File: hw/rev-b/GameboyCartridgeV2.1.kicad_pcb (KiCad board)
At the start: 4 copper layers, 52.8 x 61.2 mm, 148 parts, among them J1 USB_C_Receptacle_USB2.0, J2 Micro_SD_Card_Det2, J4 Conn_01x06, J5 CartBus, Q1 CJ2302, Q101 SIA975DJ-T1-GE3, Q102 2N7002, SW1 SW_Push, SW2 SW_Push, U1 USBLC6-2P6, U101 TPS2116DRLR, U102 TPS2553DBVR, U103 TPS63802DLAR, U104 ESP32-C3-MINI-1U-N4, U105 SN74LVC1G125DBVR, U106 SN74LVC3G34DCTR, U107 CH334P, U108 TLV3012BIDBVR, U109 TLV431BIDBZR, U2 W25Q16JVSSIQ, U3 RP2350_80QFN, U4 W956A8MBYA5I, U5 MCP79510, U6 AP2112K-3.3, U7 TXB0108PW, Y1 12MHz, Y101 12MHz 10pF 10ppm, Y2 32.768kHz

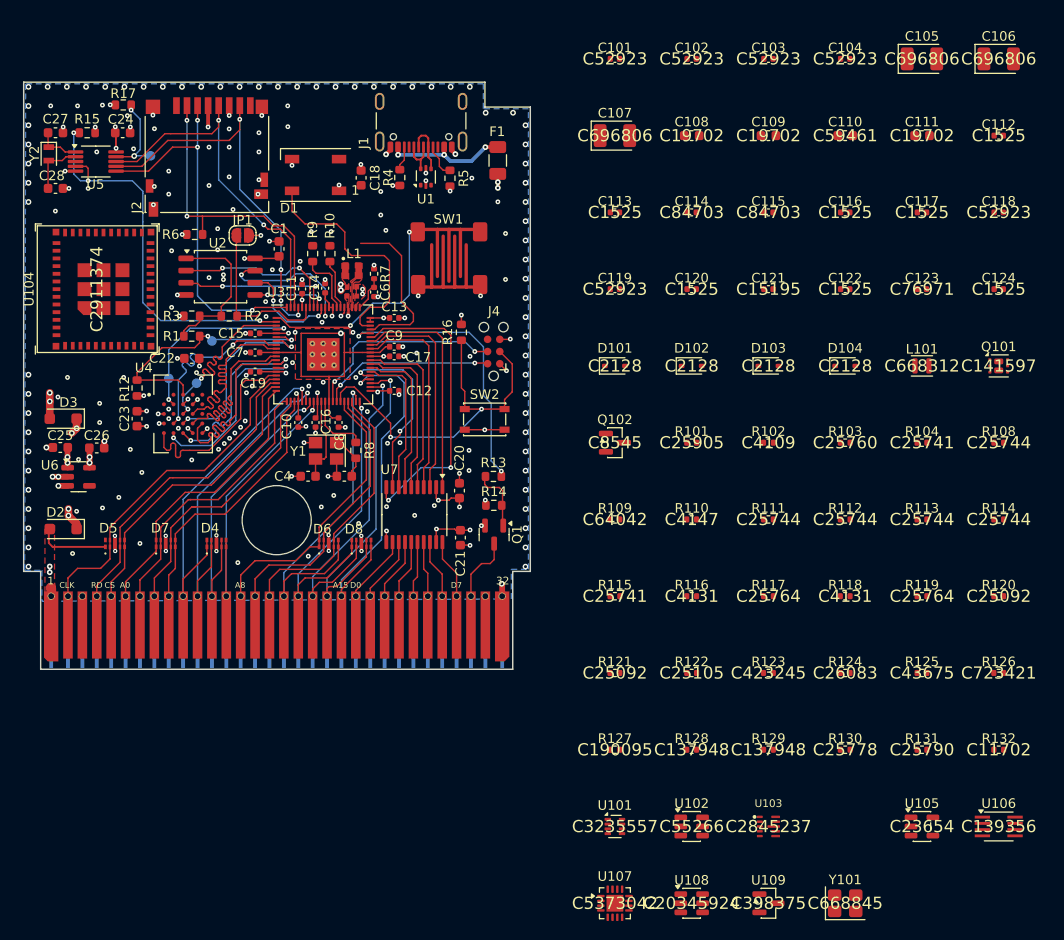
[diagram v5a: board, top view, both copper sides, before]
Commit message: layout WIP: lift tool, Croco LDO/diode cluster lifted, lower-left corner cleared; area accounting; logbook
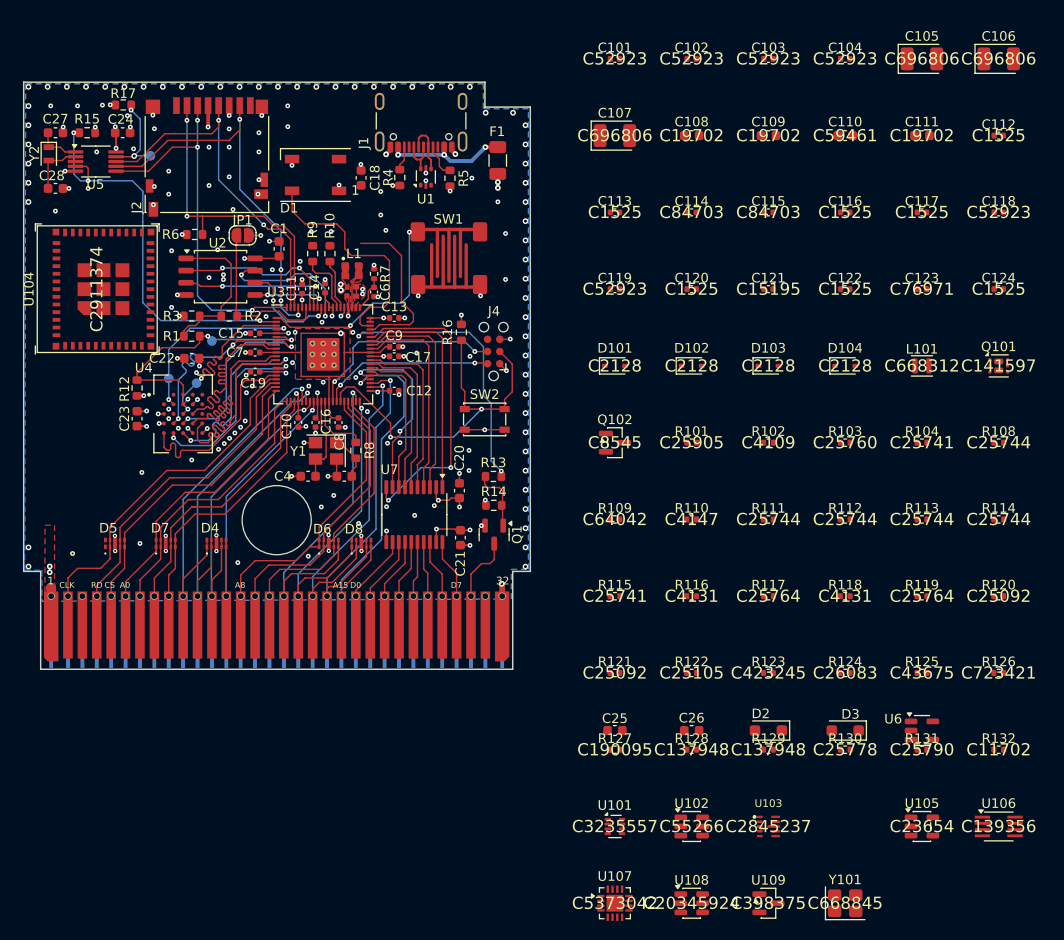
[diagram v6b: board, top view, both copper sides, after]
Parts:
- moved U6 91.8 mm to (207.0, 130.0)
- moved D3 87.7 mm to (199.0, 130.0)
- moved D2 76.4 mm to (191.0, 130.0)
- moved C26 68.6 mm to (183.0, 130.0)
- moved C25 64.9 mm to (175.0, 130.0)
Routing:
- net VCC: track 13.4 -> 5.86 mm
- net +5V: track 7.24 -> 0.00 mm, vias 7 -> 0
- net GND: track 52.6 -> 49.6 mm, vias 221 -> 198
- net VBUS: track 4.68 -> 1.98 mm, vias 5 -> 3
- net +3V3: track 48.4 -> 46.4 mm, vias 33 -> 31

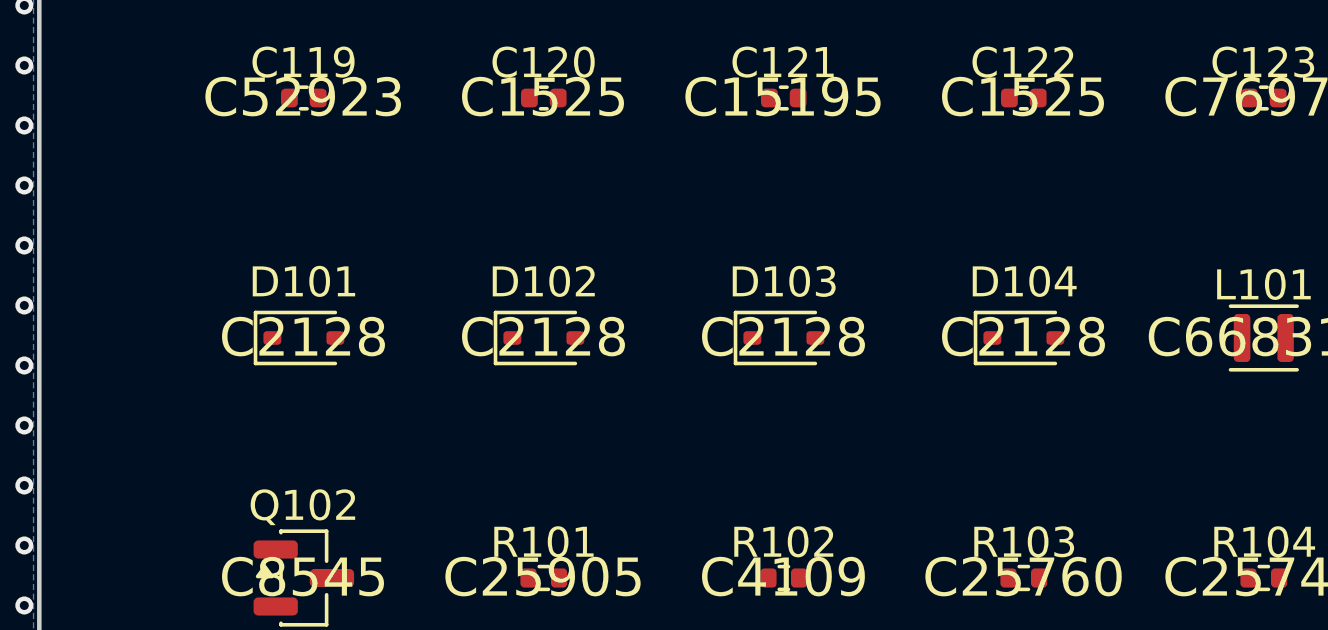
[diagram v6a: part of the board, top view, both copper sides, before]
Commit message: option A area check: does not fit; SOD-523 clamp diodes; geometry plot tools; logbook
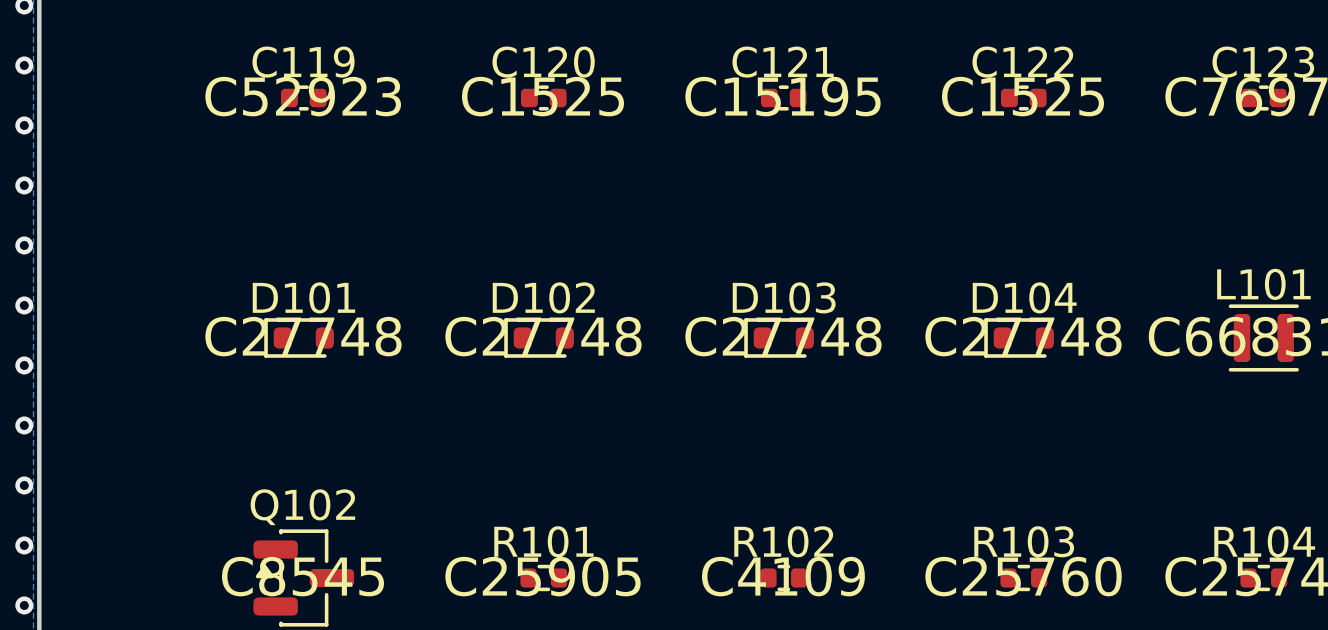
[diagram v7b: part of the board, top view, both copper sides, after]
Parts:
- D101, D102, D103, D104: value 1N4148WS -> 1N4148WT; footprint Diode_SMD:D_SOD-323 -> Diode_SMD:D_SOD-523

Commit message: board: 4 -> 6 layers, JLC06081H-7628 stackup (L1-L2 spacing unchanged), power planes moved In2 -> In4, In2/In3 free for signals
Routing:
- added copper zone on In4.Cu, net +3V3
- added copper zone on In4.Cu, net +5V
- added copper zone on In4.Cu, net VBUS
- added copper zone on In4.Cu, net VCC
- removed copper zone on In2.Cu, net +3V3
- removed copper zone on In2.Cu, net +5V
- removed copper zone on In2.Cu, net VBUS
- removed copper zone on In2.Cu, net VCC
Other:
- copper layers 4 -> 6
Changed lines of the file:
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@@
 	(generator_version "10.0")
 	(general
-		(thickness 0.7912)
+		(thickness 0.818)
 		(legacy_teardrops no)
 	)
@@
 		(4 "In1.Cu" signal)
 		(6 "In2.Cu" signal)
+		(8 "In3.Cu" signal)
+		(10 "In4.Cu" signal)
 		(2 "B.Cu" signal)
 		(9 "F.Adhes" user "F.Adhesive")
@@
 				(type "prepreg")
 				(thickness 0.2104)
-				(material "FR4")
-				(epsilon_r 4.5)
+				(material "7628")
+				(epsilon_r 4.4)
 				(loss_tangent 0.02)
 			)
@@
 			(layer "dielectric 2"
 				(type "core")
-				(thickness 0.25)
-				(material "FR4")
-				(epsilon_r 4.5)
+				(thickness 0.075)
+				(material "Core")
+				(epsilon_r 3.99)
 				(loss_tangent 0.02)
 			)
@@
 			(layer "dielectric 3"
 				(type "prepreg")
+				(thickness 0.1164)
+				(material "2116")
+				(epsilon_r 4.16)
+				(loss_tangent 0.02)
+			)
+			(layer "In3.Cu"
+				(type "copper")
+				(thickness 0.0152)
+			)
+			(layer "dielectric 4"
+				(type "core")
+				(thickness 0.075)
+				(material "Core")
+				(epsilon_r 3.99)
+				(loss_tangent 0.02)
+			)
+			(layer "In4.Cu"
+				(type "copper")
+				(thickness 0.0152)
+			)
+			(layer "dielectric 5"
+				(type "prepreg")
 				(thickness 0.2104)
-				(material "FR4")
-				(epsilon_r 4.5)
+				(material "7628")
+				(epsilon_r 4.4)
 				(loss_tangent 0.02)
 			)
@@
 				(font
 					(size 1.27 1.27)
+					(thickness 0.15)
 				)
 			)
@@
 				(font
 					(size 1.27 1.27)
+					(thickness 0.15)
 				)
 			)
@@
 				(font
 					(size 1.27 1.27)
+					(thickness 0.15)
 				)
 			)
@@
 				(font
 					(size 1.27 1.27)
+					(thickness 0.15)
 				)
 			)
@@
 		(end 146.43646 88.6)
 		(width 0.6)
-		(layer "In2.Cu")
+		(layer "In4.Cu")
 		(net "+1V1")
 	)
@@
 		(end 146.446121 88.590339)
 		(width 0.6)
-		(layer "In2.Cu")
+		(layer "In4.Cu")
 		(net "+1V1")
 	)
@@
 		(end 146.446121 86.8)
 		(width 0.6)
-		(layer "In2.Cu")
+		(layer "In4.Cu")
 		(net "+1V1")
 	)
@@
 		(end 146.425 83.5)
 		(width 0.6)
-		(layer "In2.Cu")
+		(layer "In4.Cu")
 		(net "+1V1")
 	)
@@
 		(end 146.446121 83.521121)
 		(width 0.6)
-		(layer "In2.Cu")
+		(layer "In4.Cu")
 		(net "+1V1")
 	)
@@
 	(zone
 		(net "VCC")
-		(layer "In2.Cu")
+		(layer "In4.Cu")
 		(hatch edge 0.5)
 		(priority 10)
@@
 		)
 		(min_thickness 0.15)
-		(fill yes
+		(fill
 			(thermal_gap 0.5)
 			(thermal_bridge_width 0.5)
@@
 	(zone
 		(net "+5V")
-		(layer "In2.Cu")
+		(layer "In4.Cu")
 		(hatch edge 0.5)
 		(priority 8)
@@
 		)
 		(min_thickness 0.25)
-		(fill yes
+		(fill
 			(thermal_gap 0.5)
 			(thermal_bridge_width 0.5)
@@
 	(zone
 		(net "VBUS")
-		(layer "In2.Cu")
+		(layer "In4.Cu")
 		(hatch edge 0.5)
 		(priority 3)
@@
 		)
 		(min_thickness 0.25)
-		(fill yes
+		(fill
 			(thermal_gap 0.5)
 			(thermal_bridge_width 0.5)
@@
 	(zone
 		(net "+3V3")
-		(layer "In2.Cu")
+		(layer "In4.Cu")
 		(hatch edge 0.5)
 		(priority 1)
@@
 		)
 		(min_thickness 0.2)
-		(fill yes
+		(fill
 			(thermal_gap 0.3)
 			(thermal_bridge_width 0.3)
